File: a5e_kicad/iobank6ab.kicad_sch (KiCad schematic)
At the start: 1 part, among them U7 A5EB013B-B23B

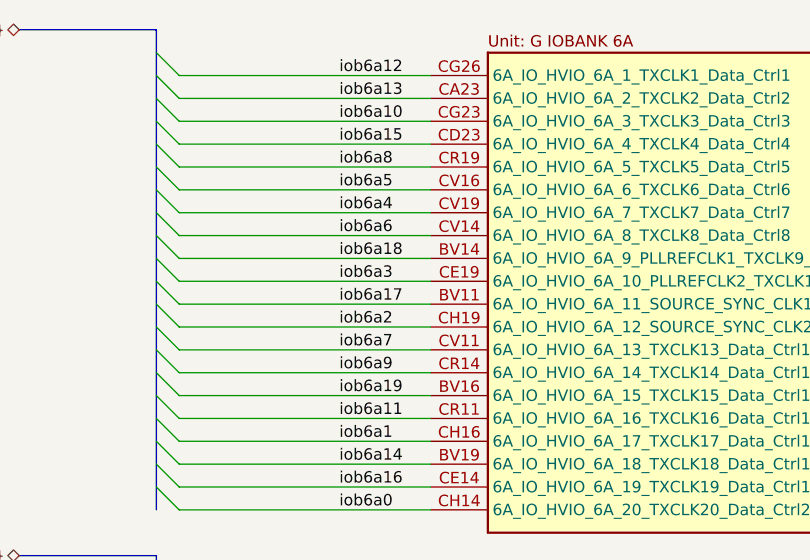
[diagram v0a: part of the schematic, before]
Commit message: fix clock routing and move all components inside board perimeters
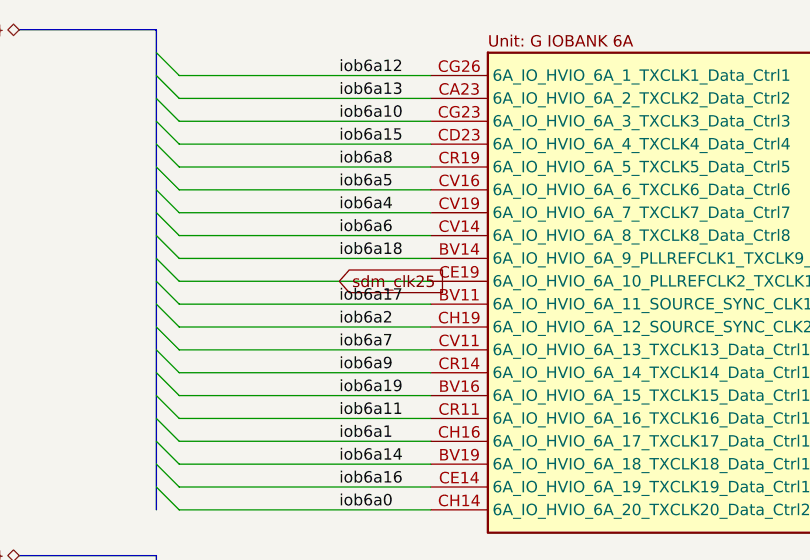
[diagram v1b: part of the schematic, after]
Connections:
- net iob6a3 renamed sdm_clk25
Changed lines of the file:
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@@
-		)
-	)
-	(label "iob6a3"
-		(at 86.36 50.8 0)
-		(effects
-			(font
-				(size 1.27 1.27)
-			)
-			(justify left bottom)
 		)
 	)
@@
 		)
 	)
+	(global_label "sdm_clk25"
+		(shape input)
+		(at 86.36 50.8 0)
+		(effects
+			(font
+				(size 1.27 1.27)
+			)
+			(justify left)
+		)
+		(property "Intersheetrefs" "${INTERSHEET_REFS}"
+			(at 86.36 50.8 0)
+			(hide yes)
+			(show_name no)
+			(do_not_autoplace no)
+			(effects
+				(font
+					(size 1.27 1.27)
+				)
+			)
+		)
+	)

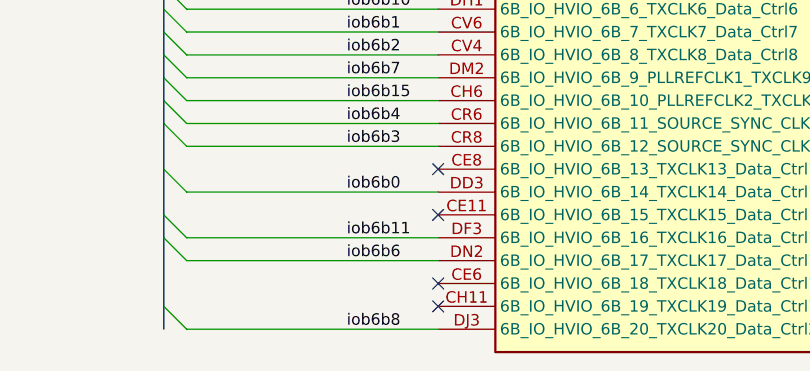
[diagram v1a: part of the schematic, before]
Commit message: add hps uart
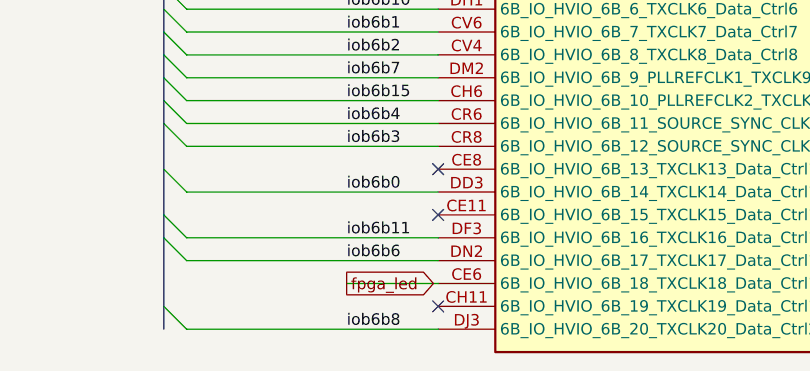
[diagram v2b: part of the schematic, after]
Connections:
- net fpga_led: now reaches U7.CE6 (6B_IO_HVIO_6B_18_TXCLK18_Data_Ctrl18)
- no-connect marks 4 -> 3
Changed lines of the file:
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@@
-	)
-	(no_connect
-		(at 96.52 129.54)
 	)
 	(no_connect
@@
 		)
 	)
+	(wire
+		(pts
+			(xy 86.36 129.54) (xy 96.52 129.54)
+		)
+		(stroke
+			(width 0)
+			(type default)
+		)
+	)
 	(bus
 		(pts
@@
 		)
 	)
+	(global_label "fpga_led"
+		(shape output)
+		(at 86.36 129.54 0)
+		(effects
+			(font
+				(size 1.27 1.27)
+			)
+			(justify left)
+		)
+		(property "Intersheetrefs" "${INTERSHEET_REFS}"
+			(at 86.36 129.54 0)
+			(hide yes)
+			(show_name no)
+			(do_not_autoplace no)
+			(effects
+				(font
+					(size 1.27 1.27)
+				)
+			)
+		)
+	)
